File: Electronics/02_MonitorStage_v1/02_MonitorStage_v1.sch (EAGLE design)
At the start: 53 parts, among them J1 BARRIER_BLOCK-2PIN, J2 BARRIER_BLOCK-2PIN, J3 CONN_2X3_SMD, J4 CONN_2X3_SMD, J5 CONN_2X3_SMD, J6 CONN_2X3_SMD, J7 CONN_2X3_SMD, Q1 PN2222A-SOT-23

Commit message: Progress on monitor electronics schematic
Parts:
- removed J1: BARRIER_BLOCK-2PIN, Hippo-PS:BARRIER_BLOCK-2PIN
- removed TP3, TP4: TP, Hippo-PS:TP
- added C2, C3: 0.1uF, standardparts:CAPACITOR.1206
- added R14, R15: 1K, standardparts:RESISTOR.1206
- added S2, S3: TACTILE_BUTTON, Hippo-PS:TACTILE_BUTTON
- C1: value (none) -> 0.1uF
- R13: value (none) -> 1K
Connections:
- new net +5V1: R1.2
- new net +5V_SIG: J6.P$3
- new net BUTTON2: C2.2, R14.2, S2.NO
- new net BUTTON3: C3.2, R15.2, S3.NO
- new net BUZZER: LS1.P$1, R2.1
- new net IN+_SIG: J6.P$1
- new net N$1: BT1.+, U$1.VBAT
- new net N$10: D9.1, R9.2
- new net N$11: D10.1, R10.2
- new net N$12: D11.1, R11.2
- new net N$13: LS1.P$2, Q1.COLLECTOR, R1.1
- new net N$14: R3.1
- new net N$15: R4.1
- new net N$16: R5.1
- new net N$17: R6.1
- new net N$18: R7.1
- new net N$19: R8.1
- new net N$2: D1.1, R3.2
- new net N$20: R9.1
- new net N$21: R10.1
- new net N$22: R11.1
- new net N$23: Q1.BASE, R2.2
- new net N$3: D2.1, R4.2
- new net N$5: D3.1, R5.2
- new net N$7: D4.1, R6.2
- new net N$8: D5.1, R7.2
- new net N$9: D6.1, R8.2
- new net S03_SIG1: J7.P$2
- new net S03_SIG2: J7.P$1
- new net S03_SIG3: J7.P$3
- new net S03_SIG4: J7.P$5
- new net S03_SIGSMPS: J7.P$4
- new net S04_SIG1: J3.P$4
- new net S04_SIG2: J3.P$5
- new net S04_SIG3: J3.P$3
- new net S04_SIGSMPS: J3.P$1
- new net S05_SIG1: J4.P$3
- new net S05_SIG2: J4.P$5
- new net S05_SIGNP: J4.P$4
- new net S05_SIGSMPS: J4.P$1
- new net S06_SIG1: J5.P$5
- new net S06_SIGSMPS: J5.P$4
- net +5V: now also J2.P$1, J6.P$4, U$1.VIN
- net GND: now also BT1.-, C2.1, C3.1, D1.2, D10.2, D11.2, D2.2, D3.2, D4.2, D5.2, D6.2, D9.2, J3.P$6, J4.P$6, J5.P$6, J6.P$6, J7.P$6, Q1.EMITTER, R14.1, R15.1, U$2.GND; no longer J1.P$2, TP4.P$1
- net IN+: no longer J2.P$1
- net N$4: now also S2.COM, S3.COM
- net V+: now also U$1.3V3, U$2.VCC; no longer J1.P$1, TP3.P$1
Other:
- note added: "Stage 01"
- note added: "Stage 03"
- note added: "Stage 04"
- note added: "Stage 05"
- note added: "Stage 06"

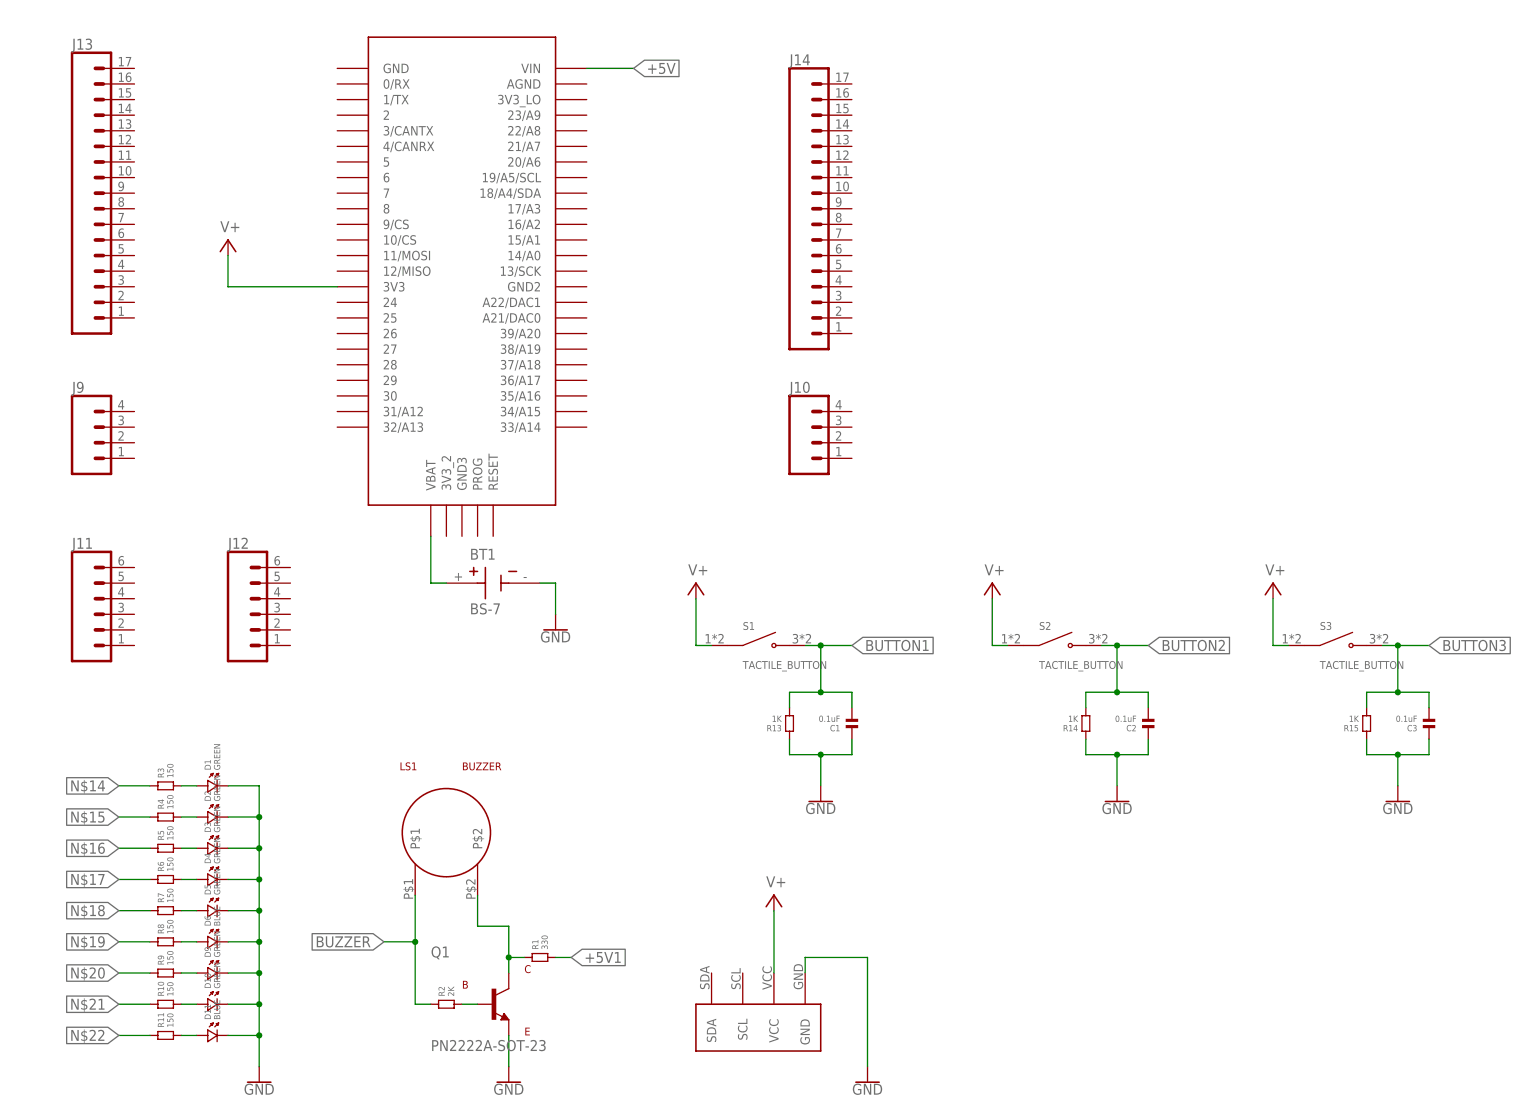
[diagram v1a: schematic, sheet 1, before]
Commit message: Routed monitor stage board
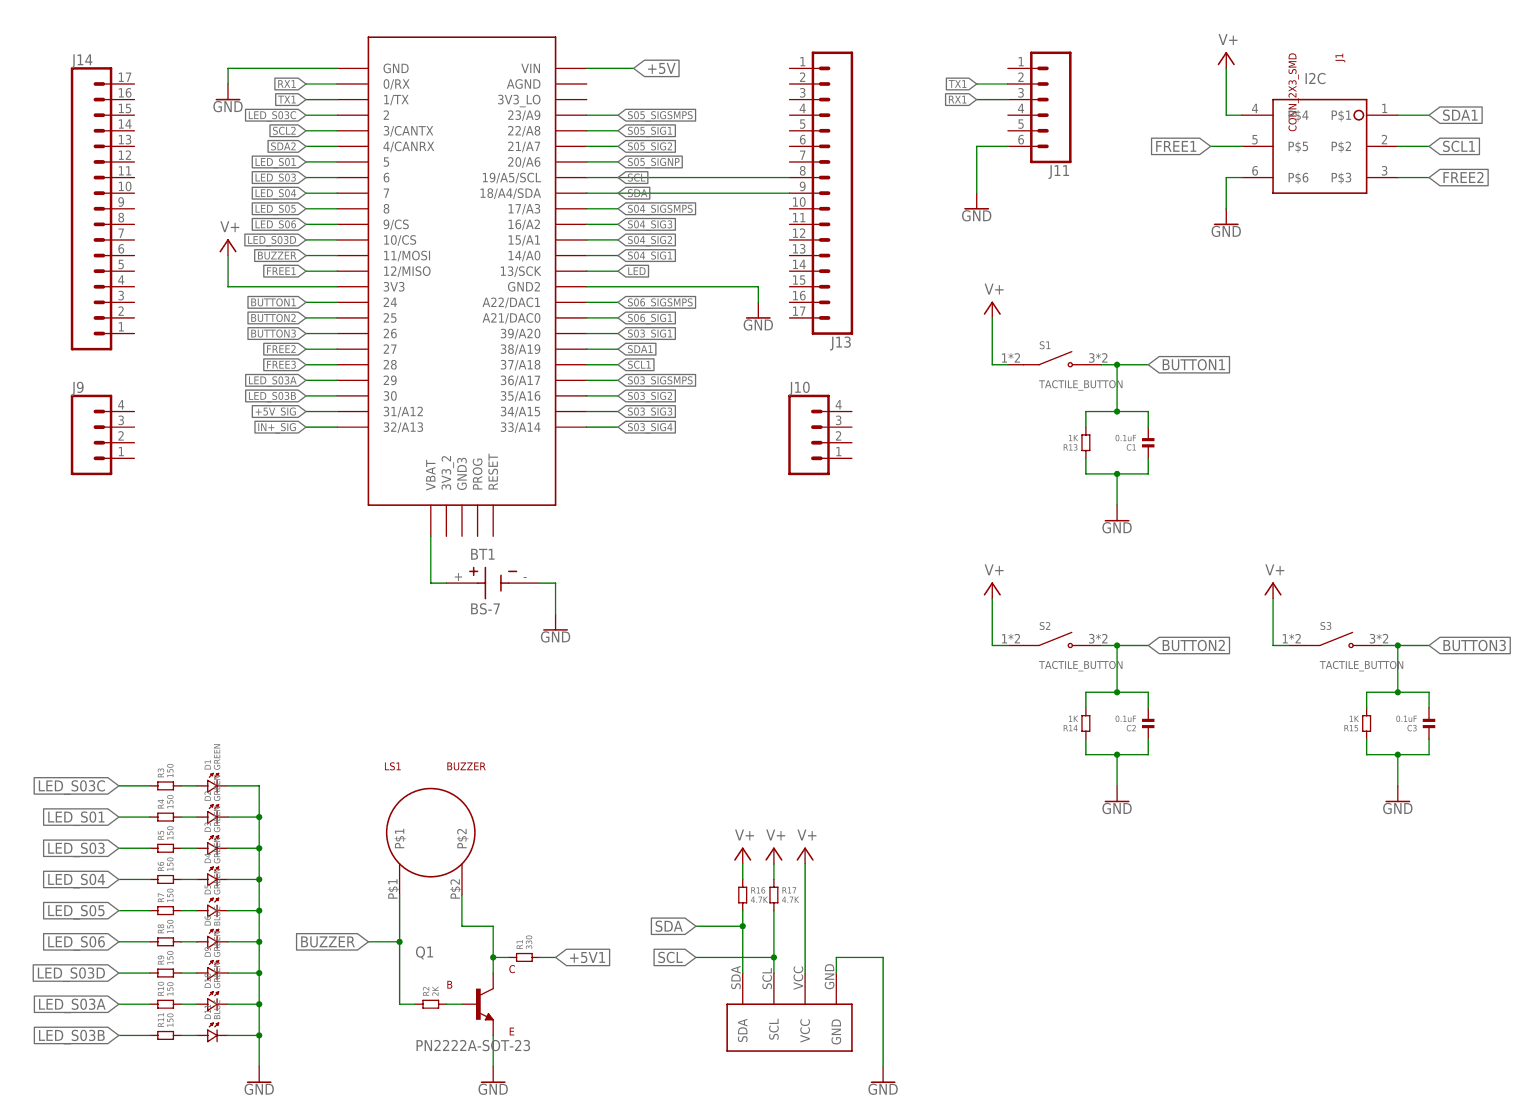
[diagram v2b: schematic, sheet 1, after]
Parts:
- removed J12: (no value), Hippo-PS:CONN_06
- added J1: CONN_2X3_SMD, Hippo-PS:CONN_2X3_SMD
- added R16, R17: 4.7K, standardparts:RESISTOR.1206
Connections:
- removed net N$14: R3.1
- removed net N$15: R4.1
- removed net N$16: R5.1
- removed net N$17: R6.1
- removed net N$18: R7.1
- removed net N$19: R8.1
- removed net N$20: R9.1
- removed net N$21: R10.1
- removed net N$22: R11.1
- removed net N$4: S1.COM, S2.COM, S3.COM
- new net FREE1: J1.P$5, U$1.12/MISO
- new net FREE2: J1.P$3, U$1.27
- new net FREE3: U$1.28
- new net LED: U$1.13/SCK
- new net LED_S01: R4.1, U$1.5
- new net LED_S03: R5.1, U$1.6
- new net LED_S03A: R10.1, U$1.29
- new net LED_S03B: R11.1, U$1.30
- new net LED_S03C: R3.1, U$1.2
- new net LED_S03D: R9.1, U$1.10/CS
- new net LED_S04: R6.1, U$1.7
- new net LED_S05: R7.1, U$1.8
- new net LED_S06: R8.1, U$1.9/CS
- new net RX1: J11.3, U$1.0/RX
- new net SCL: J13.8, R17.2, U$1.19/A5/SCL, U$2.SCL
- new net SCL1: J1.P$2, U$1.37/A18
- new net SCL2: U$1.3/CANTX
- new net SDA: J13.9, R16.2, U$1.18/A4/SDA, U$2.SDA
- new net SDA1: J1.P$1, U$1.38/A19
- new net SDA2: U$1.4/CANRX
- new net TX1: J11.2, U$1.1/TX
- net +5V_SIG: now also U$1.31/A12
- net BUTTON1: now also U$1.24
- net BUTTON2: now also U$1.25
- net BUTTON3: now also U$1.26
- net BUZZER: now also U$1.11/MOSI
- net GND: now also J1.P$6, J11.6, U$1.GND, U$1.GND2
- net IN+_SIG: now also U$1.32/A13
- net S03_SIG1: now also U$1.39/A20
- net S03_SIG2: now also U$1.35/A16
- net S03_SIG3: now also U$1.34/A15
- net S03_SIG4: now also U$1.33/A14
- net S03_SIGSMPS: now also U$1.36/A17
- net S04_SIG1: now also U$1.14/A0
- net S04_SIG2: now also U$1.15/A1
- net S04_SIG3: now also U$1.16/A2
- net S04_SIGSMPS: now also U$1.17/A3
- net S05_SIG1: now also U$1.22/A8
- net S05_SIG2: now also U$1.21/A7
- net S05_SIGNP: now also U$1.20/A6
- net S05_SIGSMPS: now also U$1.23/A9
- net S06_SIG1: now also U$1.A21/DAC0
- net S06_SIGSMPS: now also U$1.A22/DAC1
- net V+: now also J1.P$4, R16.1, R17.1, S1.COM, S2.COM, S3.COM
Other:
- note added: "I2C"
- moved on the sheet: C1, J11, J13, J14, LS1, Q1, R1, R13, R2, S1

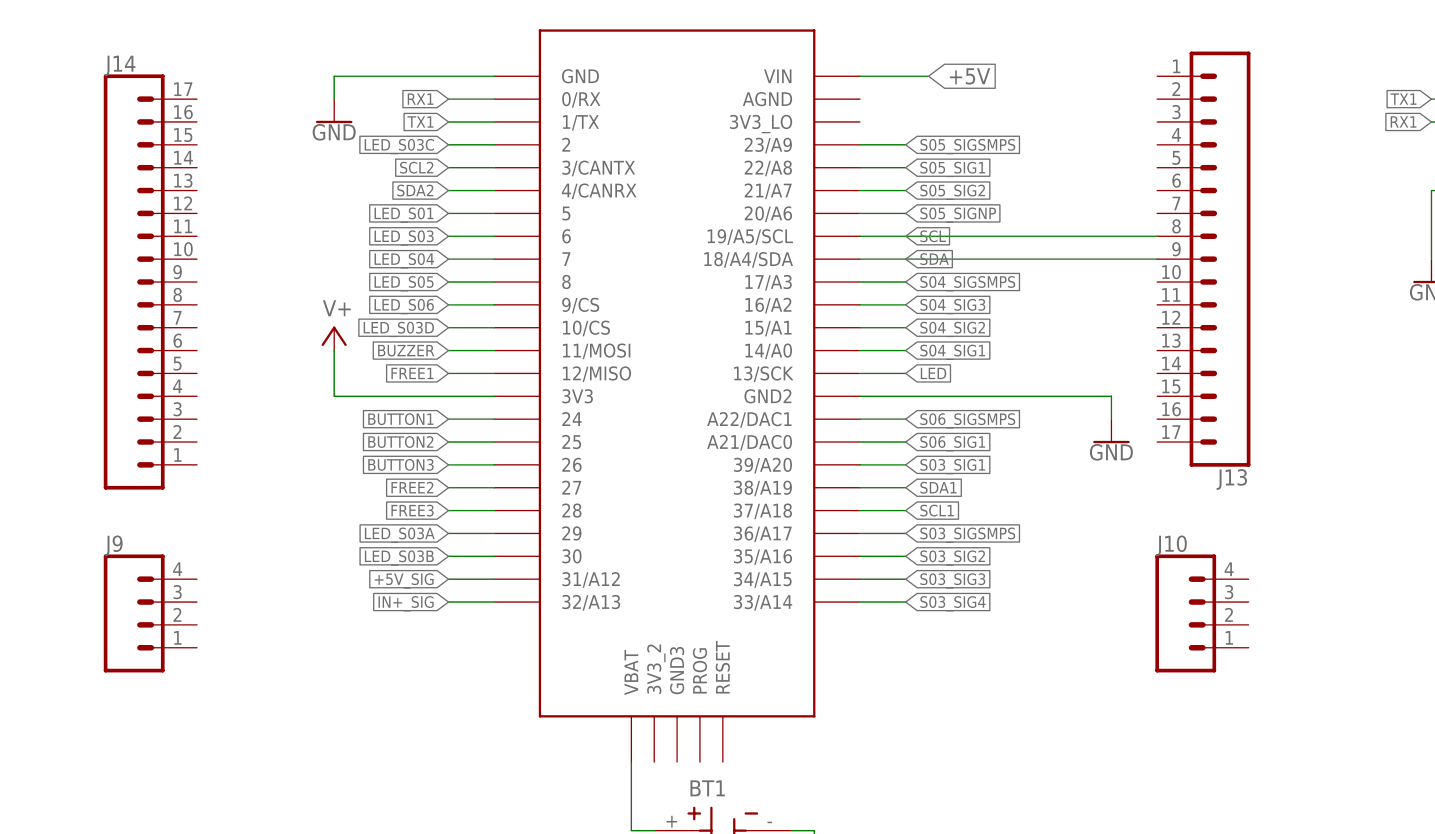
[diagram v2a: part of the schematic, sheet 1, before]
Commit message: Routing improvements on monitor stage electronics
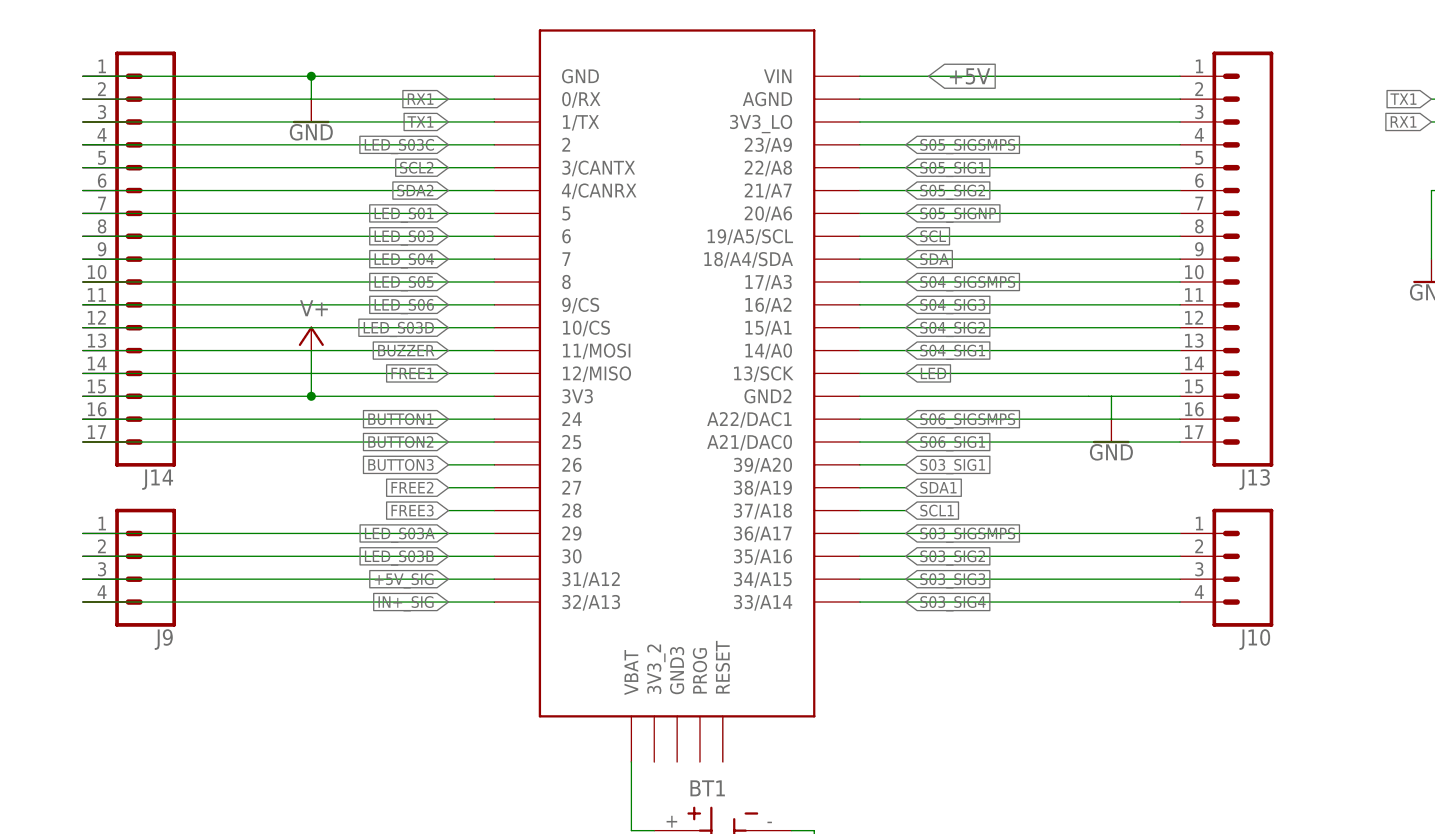
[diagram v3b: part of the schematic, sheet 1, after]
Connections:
- new net N$14: J13.3, U$1.3V3_LO
- new net N$4: J13.2, U$1.AGND
- net +5V: now also J13.1
- net +5V_SIG: now also J9.3
- net BUTTON1: now also J14.16
- net BUTTON2: now also J14.17
- net BUZZER: now also J14.13
- net FREE1: now also J14.14
- net GND: now also J13.15, J14.1
- net IN+_SIG: now also J9.4
- net LED: now also J13.14
- net LED_S01: now also J14.7
- net LED_S03: now also J14.8
- net LED_S03A: now also J9.1
- net LED_S03B: now also J9.2
- net LED_S03C: now also J14.4
- net LED_S03D: now also J14.12
- net LED_S04: now also J14.9
- net LED_S05: now also J14.10
- net LED_S06: now also J14.11
- net RX1: now also J14.2
- net S03_SIG2: now also J10.2
- net S03_SIG3: now also J10.3
- net S03_SIG4: now also J10.4
- net S03_SIGSMPS: now also J10.1
- net S04_SIG1: now also J13.13
- net S04_SIG2: now also J13.12
- net S04_SIG3: now also J13.11
- net S04_SIGSMPS: now also J13.10
- net S05_SIG1: now also J13.5
- net S05_SIG2: now also J13.6
- net S05_SIGNP: now also J13.7
- net S05_SIGSMPS: now also J13.4
- net S06_SIG1: now also J13.17
- net S06_SIGSMPS: now also J13.16
- net SCL2: now also J14.5
- net SDA2: now also J14.6
- net TX1: now also J14.3
- net V+: now also J14.15
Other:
- moved on the sheet: J10, J13, J14, J9

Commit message: Monitor stage electronics v1 final
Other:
- note added: "Brass Standoffs"
- note added: "Button"
- note added: "Buttons"
- note added: "Buzzer"
- note added: "Debug Header"
- note added: "Hippo-PD Monitor Stage Designed by: Erin Kennedy July 22, 2022"
- note added: "I2C Header"
- note added: "Input and Test Points"
- note added: "OLED Screen"
- note added: "Stage Connectors"
- note added: "Stage Status LEDs"
- note added: "Teensy 3.6"
- moved on the sheet: BT1, C1, C2, C3, D1, D10, D11, D2, D3, D4, D5, D6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

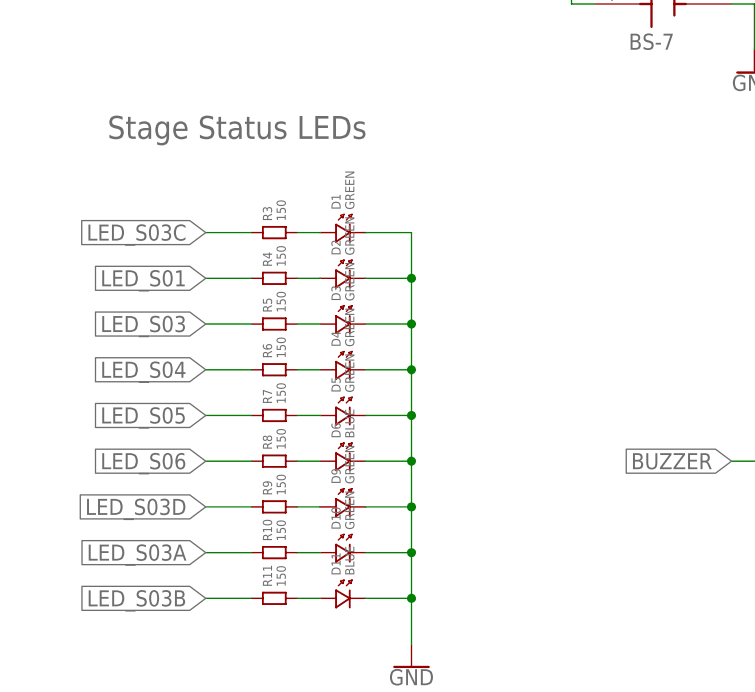
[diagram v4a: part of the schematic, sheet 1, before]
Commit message: Updated refdes of some components
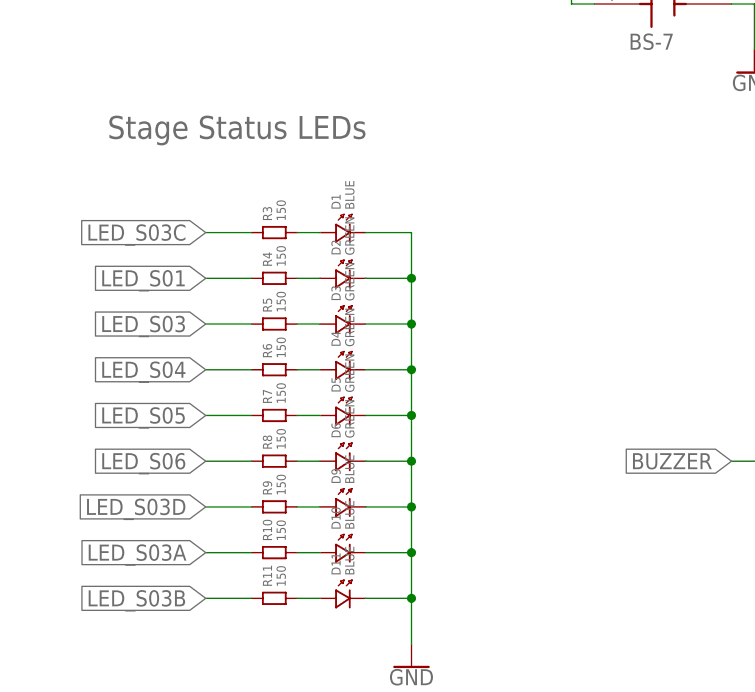
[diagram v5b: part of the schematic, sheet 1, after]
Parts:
- D1, D10, D9: value GREEN -> BLUE
- D6: value BLUE -> GREEN
- renumbered U$1 to U1, U$2 to U2
